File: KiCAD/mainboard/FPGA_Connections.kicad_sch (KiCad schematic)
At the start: 1 part, among them J2 AHDF15A-KG-TAXB

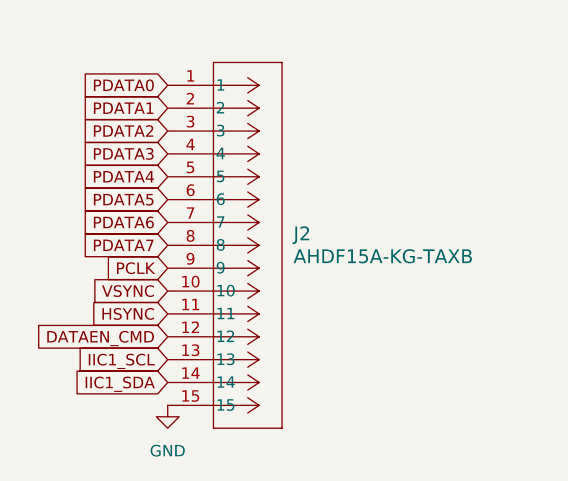
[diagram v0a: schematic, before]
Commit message: fixed pdata bus connection
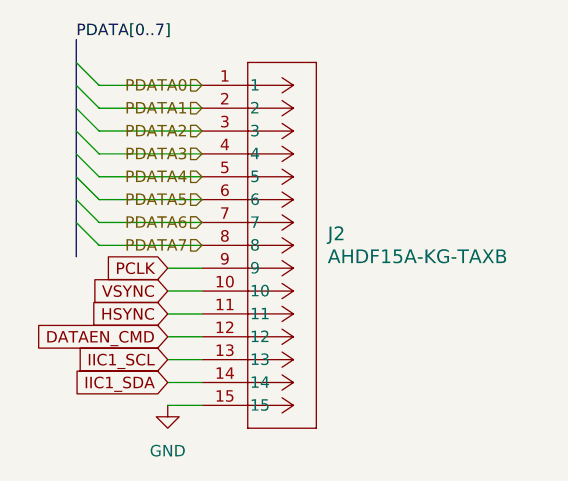
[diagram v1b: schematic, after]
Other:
- moved on the sheet: J2

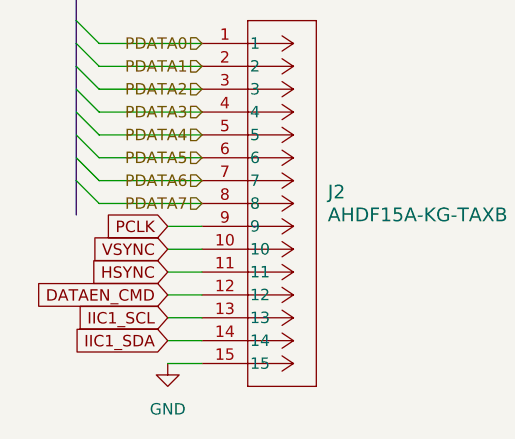
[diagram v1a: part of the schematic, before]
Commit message: fixed funny bus connectinos
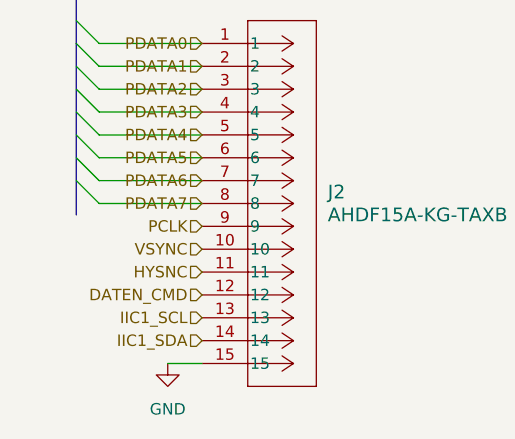
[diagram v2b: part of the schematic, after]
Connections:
- net DATAEN_CMD renamed DATEN_CMD
- net HSYNC renamed HYSNC
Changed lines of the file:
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@@
-		)
-	)
-	(wire
-		(pts
-			(xy 171.45 100.33) (xy 167.64 100.33)
-		)
-		(stroke
-			(width 0)
-			(type default)
 		)
 	)
@@
 		)
 	)
-	(wire
-		(pts
-			(xy 171.45 95.25) (xy 167.64 95.25)
-		)
-		(stroke
-			(width 0)
-			(type default)
-		)
-	)
 	(bus
 		(pts
@@
 	(wire
 		(pts
-			(xy 171.45 107.95) (xy 167.64 107.95)
-		)
-		(stroke
-			(width 0)
-			(type default)
-		)
-	)
-	(wire
-		(pts
 			(xy 160.02 87.63) (xy 171.45 87.63)
 		)
@@
 		)
 	)
-	(wire
-		(pts
-			(xy 171.45 102.87) (xy 167.64 102.87)
-		)
-		(stroke
-			(width 0)
-			(type default)
-		)
-	)
 	(bus
 		(pts
@@
 	(wire
 		(pts
-			(xy 171.45 105.41) (xy 167.64 105.41)
-		)
-		(stroke
-			(width 0)
-			(type default)
-		)
-	)
-	(wire
-		(pts
 			(xy 160.02 92.71) (xy 171.45 92.71)
 		)
@@
 		(pts
 			(xy 160.02 85.09) (xy 171.45 85.09)
-		)
-		(stroke
-			(width 0)
-			(type default)
-		)
-	)
-	(wire
-		(pts
-			(xy 171.45 97.79) (xy 167.64 97.79)
 		)
 		(stroke
@@
 		)
 	)
-	(global_label "DATAEN_CMD"
-		(shape input)
-		(at 167.64 102.87 180)
-		(fields_autoplaced yes)
-		(effects
-			(font
-				(size 1.27 1.27)
-			)
-			(justify right)
-		)
-		(property "Intersheetrefs" "${INTERSHEET_REFS}"
-			(at 152.8015 102.87 0)
-			(effects
-				(font
-					(size 1.27 1.27)
-				)
-				(justify right)
-				(hide yes)
-			)
-		)
-	)
-	(global_label "IIC1_SCL"
-		(shape input)
-		(at 167.64 105.41 180)
-		(fields_autoplaced yes)
-		(effects
-			(font
-				(size 1.27 1.27)
-			)
-			(justify right)
-		)
-		(property "Intersheetrefs" "${INTERSHEET_REFS}"
-			(at 156.4905 105.41 0)
-			(effects
-				(font
-					(size 1.27 1.27)
-				)
-				(justify right)
-				(hide yes)
-			)
-		)
-	)
-	(global_label "IIC1_SDA"
-		(shape input)
-		(at 167.64 107.95 180)
-		(fields_autoplaced yes)
-		(effects
-			(font
-				(size 1.27 1.27)
-			)
-			(justify right)
-		)
-		(property "Intersheetrefs" "${INTERSHEET_REFS}"
-			(at 156.43 107.95 0)
-			(effects
-				(font
-					(size 1.27 1.27)
-				)
-				(justify right)
-				(hide yes)
-			)
-		)
-	)
-	(global_label "PCLK"
-		(shape input)
-		(at 167.64 95.25 180)
-		(fields_autoplaced yes)
-		(effects
-			(font
-				(size 1.27 1.27)
-			)
-			(justify right)
-		)
-		(property "Intersheetrefs" "${INTERSHEET_REFS}"
-			(at 159.8167 95.25 0)
-			(effects
-				(font
-					(size 1.27 1.27)
-				)
-				(justify right)
-				(hide yes)
-			)
-		)
-	)
-	(global_label "VSYNC"
-		(shape input)
-		(at 167.64 97.79 180)
-		(fields_autoplaced yes)
-		(effects
-			(font
-				(size 1.27 1.27)
-			)
-			(justify right)
-		)
-		(property "Intersheetrefs" "${INTERSHEET_REFS}"
-			(at 158.6676 97.79 0)
-			(effects
-				(font
-					(size 1.27 1.27)
-				)
-				(justify right)
-				(hide yes)
-			)
-		)
-	)
-	(global_label "HSYNC"
-		(shape input)
-		(at 167.64 100.33 180)
-		(fields_autoplaced yes)
-		(effects
-			(font
-				(size 1.27 1.27)
-			)
-			(justify right)
-		)
-		(property "Intersheetrefs" "${INTERSHEET_REFS}"
-			(at 158.4257 100.33 0)
-			(effects
-				(font
-					(size 1.27 1.27)
-				)
-				(justify right)
-				(hide yes)
-			)
+	(hierarchical_label "IIC1_SDA"
+		(shape input)
+		(at 171.45 107.95 180)
+		(effects
+			(font
+				(size 1.27 1.27)
+			)
+			(justify right)
+		)
+	)
+	(hierarchical_label "IIC1_SCL"
+		(shape input)
+		(at 171.45 105.41 180)
+		(effects
+			(font
+				(size 1.27 1.27)
+			)
+			(justify right)
 		)
 	)
@@
 		)
 	)
+	(hierarchical_label "VSYNC"
+		(shape input)
+		(at 171.45 97.79 180)
+		(effects
+			(font
+				(size 1.27 1.27)
+			)
+			(justify right)
+		)
+	)
+	(hierarchical_label "HYSNC"
+		(shape input)
+		(at 171.45 100.33 180)
+		(effects
+			(font
+				(size 1.27 1.27)
+			)
+			(justify right)
+		)
+	)
 	(hierarchical_label "PDATA4"
 		(shape input)
@@
 		)
 	)
+	(hierarchical_label "DATEN_CMD"
+		(shape input)
+		(at 171.45 102.87 180)
+		(effects
+			(font
+				(size 1.27 1.27)
+			)
+			(justify right)
+		)
+	)
 	(hierarchical_label "PDATA1"
 		(shape input)
@@
 		(effects
 			(font
+				(size 1.27 1.27)
+			)
+			(justify right)
+		)
+	)
+	(hierarchical_label "PCLK"
+		(shape input)
+		(at 171.45 95.25 180)
+		(effects
+			(font

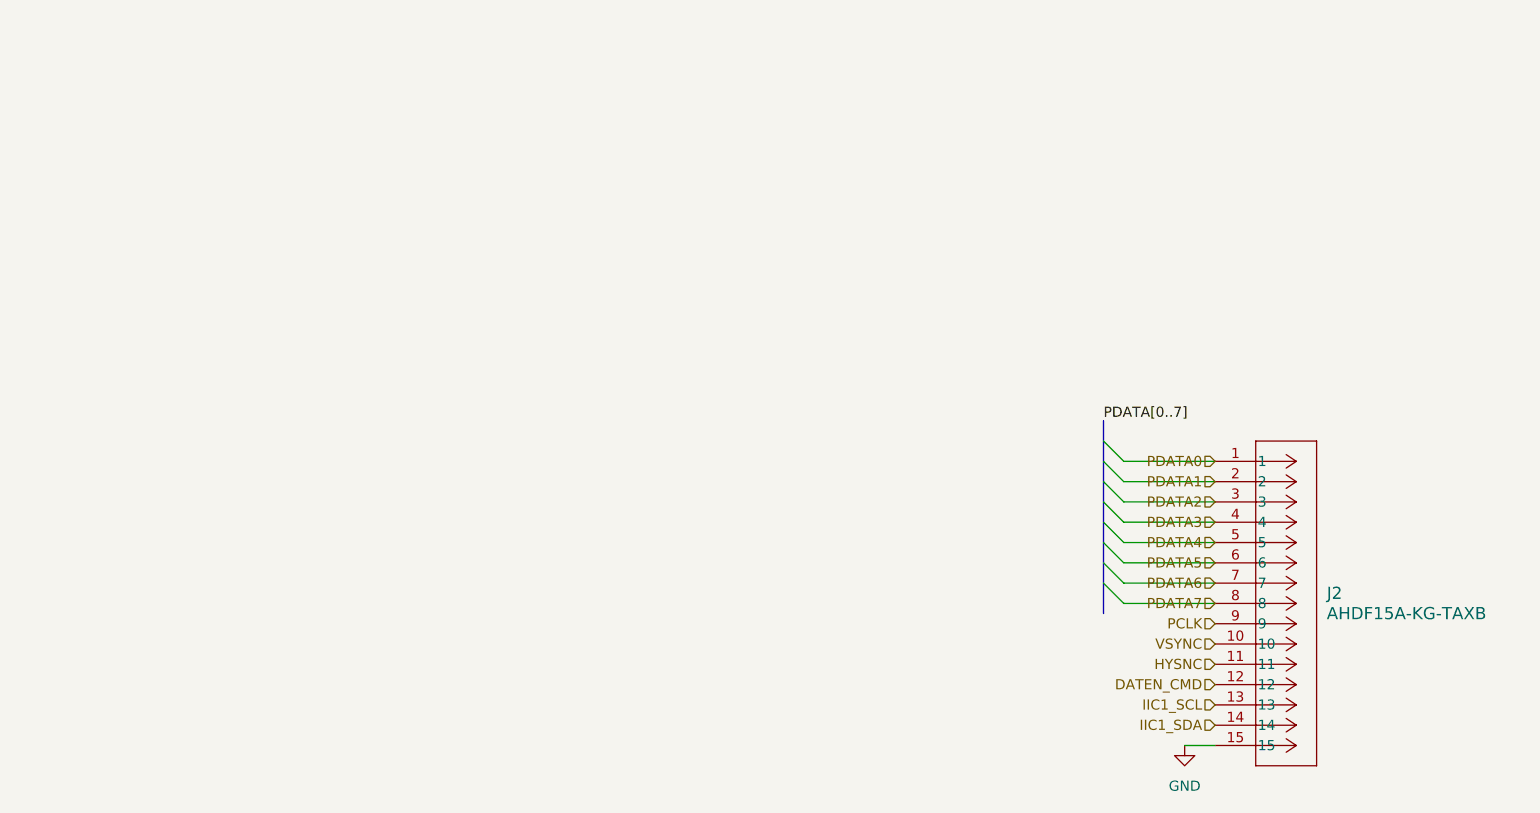
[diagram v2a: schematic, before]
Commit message: gpios are now hierarchicals
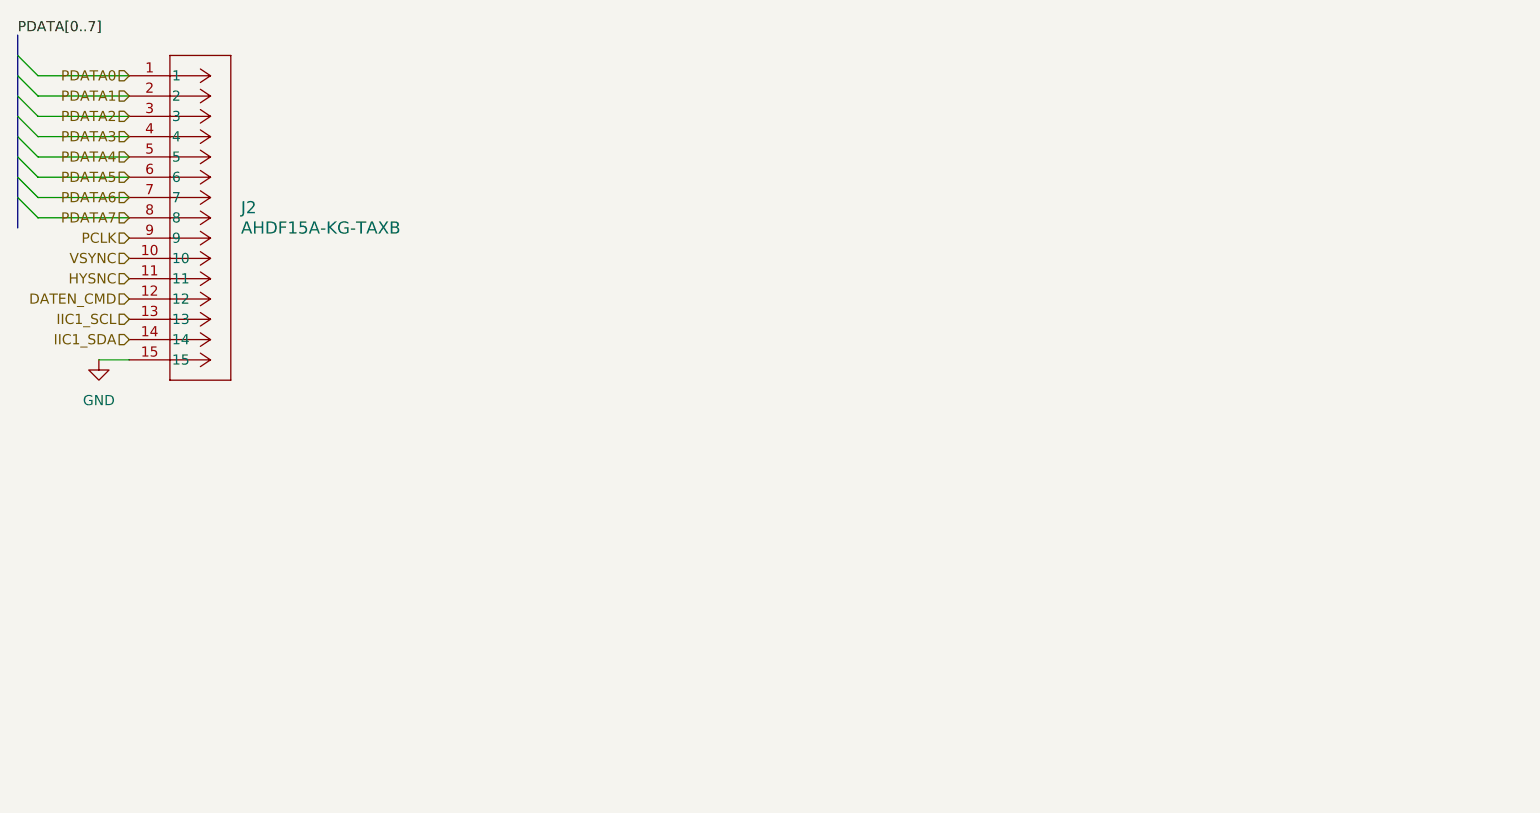
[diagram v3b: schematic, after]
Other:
- moved on the sheet: J2

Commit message: fixed all proj specific compoents
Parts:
- removed J2: AHDF15A-KG-TAXB, footprints:CONN_AHDF15A-KG-TAXB_ASM, symbol CONN_AHDF15A-KG-TAXB_ASM:AHDF15A-KG-TAXB
- added J2: AHDF15A-KG-TAXB, tp_library:AHDF15AKGTAXB, symbol tp_library:AHDF15A-KG-TAXB
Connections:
- net DATEN_CMD: now also J2.12
- net GND: now also J2.15
- net HYSNC: now also J2.11
- net IIC1_SCL: now also J2.13
- net IIC1_SDA: now also J2.14
- net PCLK: now also J2.9
- net PDATA0: now also J2.1
- net PDATA1: now also J2.2
- net PDATA2: now also J2.3
- net PDATA3: now also J2.4
- net PDATA4: now also J2.5
- net PDATA5: now also J2.6
- net PDATA6: now also J2.7
- net PDATA7: now also J2.8
- net VSYNC: now also J2.10
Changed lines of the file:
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@@
+	)
+	(symbol
+		(lib_id "tp_library:AHDF15A-KG-TAXB")
+		(at 35.56 41.91 0)
+		(unit 1)
+		(exclude_from_sim no)
+		(in_bom yes)
+		(on_board yes)
+		(dnp no)
+		(fields_autoplaced yes)
+		(property "Reference" "J2"
+			(at 49.53 41.9099 0)
+			(effects
+				(font
+					(size 1.524 1.524)
+				)
+				(justify left)
+			)
+		)
+		(property "Value" "AHDF15A-KG-TAXB"
+			(at 49.53 44.4499 0)
+			(effects
+				(font
+					(size 1.524 1.524)
+				)
+				(justify left)
+			)
+		)
+		(property "Footprint" "tp_library:AHDF15AKGTAXB"
+			(at 49.53 46.9899 0)
+			(effects
+				(font
+					(size 1.27 1.27)
+					(italic yes)
+				)
+				(justify left)
+			)
+		)
+		(property "Datasheet" "AHDF15A-KG-TAXB"
+			(at 34.544 17.018 0)
+			(effects
+				(font
+					(size 1.27 1.27)
+					(italic yes)
+				)
+				(hide yes)
+			)
+		)
+		(property "Description" ""
+			(at 35.56 41.91 0)
+			(effects
+				(font
+					(size 1.27 1.27)
+				)
+				(hide yes)
+			)
+		)
+		(pin "1"
+		)
+		(pin "12"
+		)
+		(pin "7"
+		)
+		(pin "2"
+		)
+		(pin "10"
+		)
+		(pin "6"
+		)
+		(pin "4"
+		)
+		(pin "11"
+		)
+		(pin "14"
+		)
+		(pin "3"
+		)
+		(pin "9"
+		)
+		(pin "13"
+		)
+		(pin "15"
+		)
+		(pin "8"
+		)
+		(pin "5"
+		)
+		(instances
+			(project ""
+				(path "/38e83f42-2cf9-4799-a46f-ca415d95b90a/d9917a32-1639-4a8c-8be9-7890da258af1"
+					(reference "J2")
+					(unit 1)
+				)
+			)
+		)
 	)
 	(symbol
@@
 					(unit 1)
 				)
-			)
-		)
-	)
-	(symbol
-		(lib_id "CONN_AHDF15A-KG-TAXB_ASM:AHDF15A-KG-TAXB")
-		(at 35.56 26.67 0)
-		(unit 1)
-		(exclude_from_sim no)
-		(in_bom yes)
-		(on_board yes)
-		(dnp no)
-		(fields_autoplaced yes)
-		(property "Reference" "J2"
-			(at 49.53 43.1799 0)
-			(effects
-				(font
-					(size 1.524 1.524)
-				)
-				(justify left)
-			)
-		)
-		(property "Value" "AHDF15A-KG-TAXB"
-			(at 49.53 45.7199 0)
-			(effects
-				(font
-					(size 1.524 1.524)
-				)
-				(justify left)
-			)
-		)
-		(property "Footprint" "footprints:CONN_AHDF15A-KG-TAXB_ASM"
-			(at 34.036 22.606 0)
-			(effects
-				(font
-					(size 1.27 1.27)
-					(italic yes)
-				)
-				(hide yes)
-			)
-		)
-		(property "Datasheet" "AHDF15A-KG-TAXB"
-			(at 34.544 17.018 0)
-			(effects
-				(font
-					(size 1.27 1.27)
-					(italic yes)
-				)
-				(hide yes)
-			)
-		)
-		(property "Description" ""
-			(at 35.56 26.67 0)
-			(effects
-				(font
-					(size 1.27 1.27)
-				)
-				(hide yes)
-			)
-		)
-		(pin "4"
-		)
-		(pin "3"
-		)
-		(pin "6"
-		)
-		(pin "5"
-		)
-		(pin "2"
-		)
-		(pin "1"
-		)
-		(pin "10"
-		)
-		(pin "9"
-		)
-		(pin "15"
-		)
-		(pin "14"
-		)
-		(pin "13"
-		)
-		(pin "12"
-		)
-		(pin "11"
-		)
-		(pin "8"
-		)
-		(pin "7"
-		)
-		(instances
-			(project "mainboard"
-				(path "/38e83f42-2cf9-4799-a46f-ca415d95b90a/d9917a32-1639-4a8c-8be9-7890da258af1"
-					(reference "J2")
-					(unit 1)
-				)

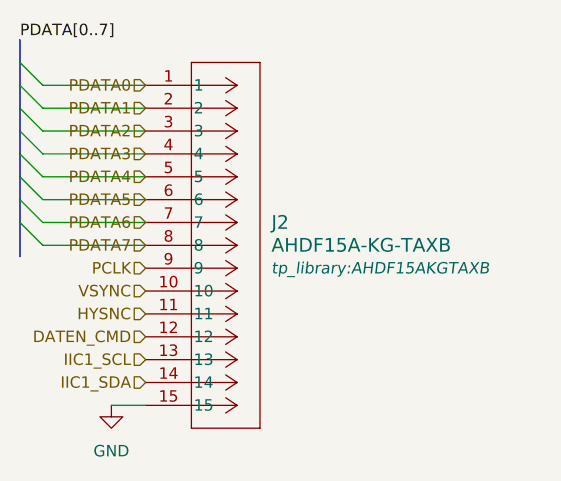
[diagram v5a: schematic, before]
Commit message: changes to all schematic files fixing ERC errors
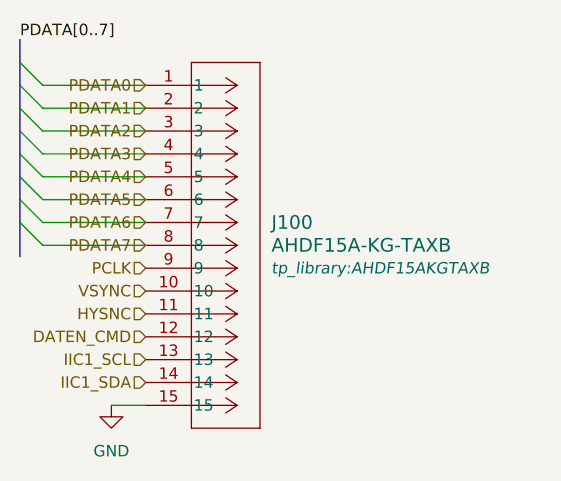
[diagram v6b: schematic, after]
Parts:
- renumbered J2 to J100
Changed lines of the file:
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@@
 		(dnp no)
 		(fields_autoplaced yes)
-		(property "Reference" "J2"
+		(property "Reference" "J100"
 			(at 49.53 41.9099 0)
 			(effects
@@
 			(project ""
 				(path "/38e83f42-2cf9-4799-a46f-ca415d95b90a/d9917a32-1639-4a8c-8be9-7890da258af1"
-					(reference "J2")
+					(reference "J100")
 					(unit 1)
 				)

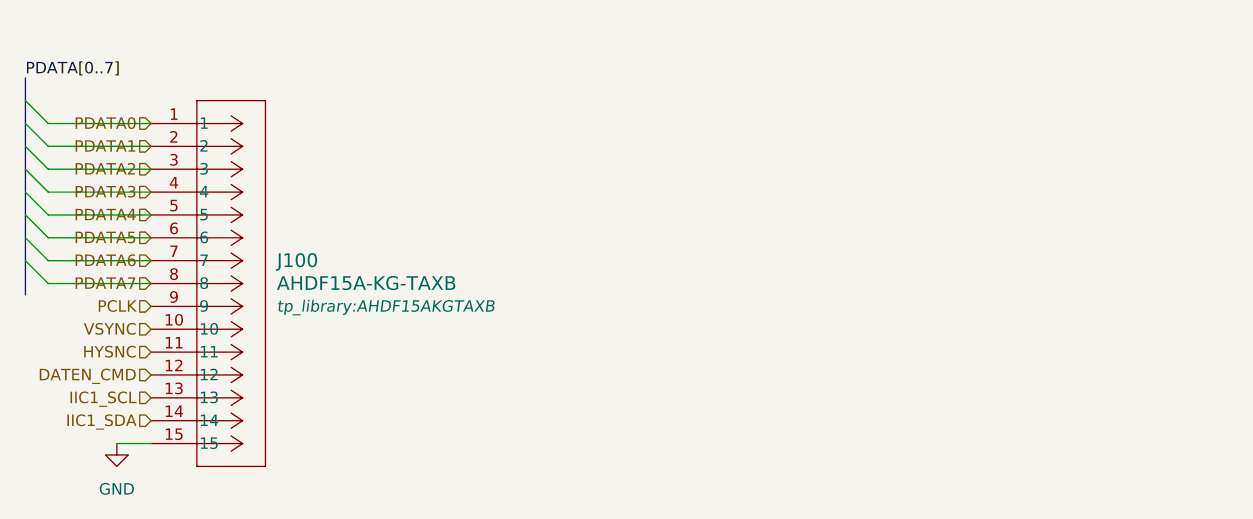
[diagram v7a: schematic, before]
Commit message: schematic changes - zero DRC errors but I have things to dicuss, and layout footprint work and rearrangment
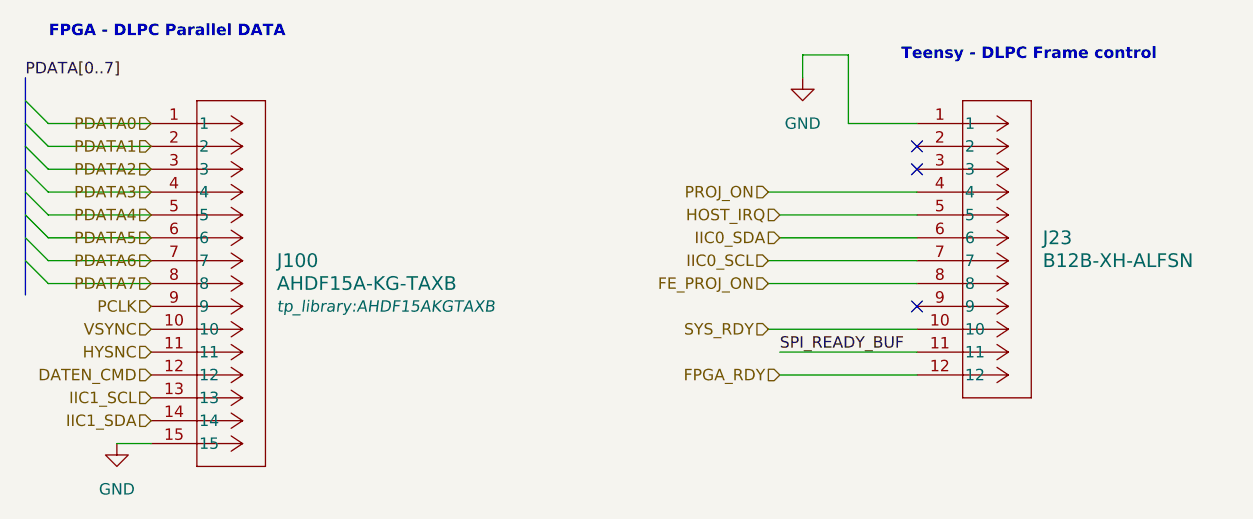
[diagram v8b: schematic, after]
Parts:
- added J23: B12B-XH-ALFSN, tp_library:B12B-XH-A-LF-SN-, symbol B12B-XH-A-LF-SN-:B12B-XH-ALFSN
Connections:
- net GND: now also J23.1
- new net FE_PROJ_ON: J23.8
- new net FPGA_RDY: J23.12
- new net HOST_IRQ: J23.5
- new net IIC0_SCL: J23.7
- new net IIC0_SDA: J23.6
- new net PROJ_ON: J23.4
- new net SPI_READY_BUF: J23.11
- new net SYS_RDY: J23.10
- no-connect marks 0 -> 3
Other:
- note added: "FPGA - DLPC Parallel DATA"
- note added: "Teensy - DLPC Frame control"
